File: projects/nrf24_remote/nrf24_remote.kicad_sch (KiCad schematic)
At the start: 74 parts

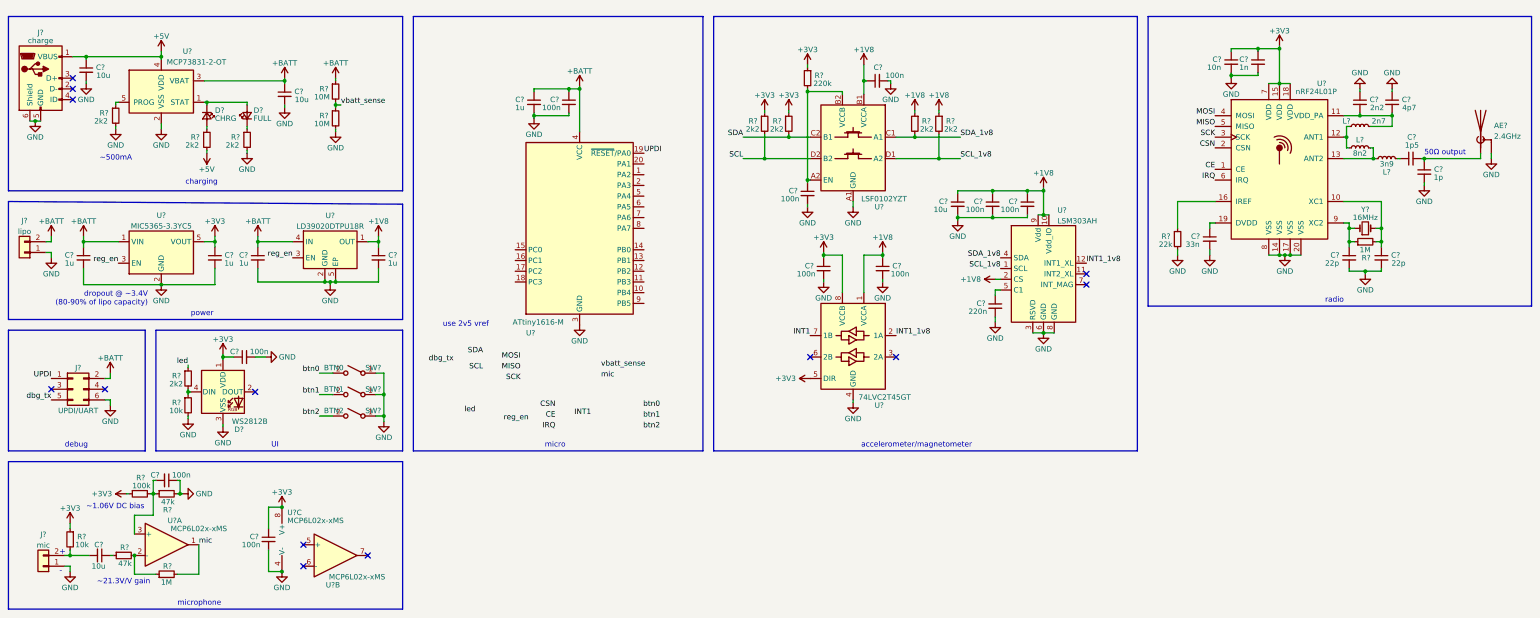
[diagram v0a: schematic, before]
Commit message: assigned nrf24_remote footprints
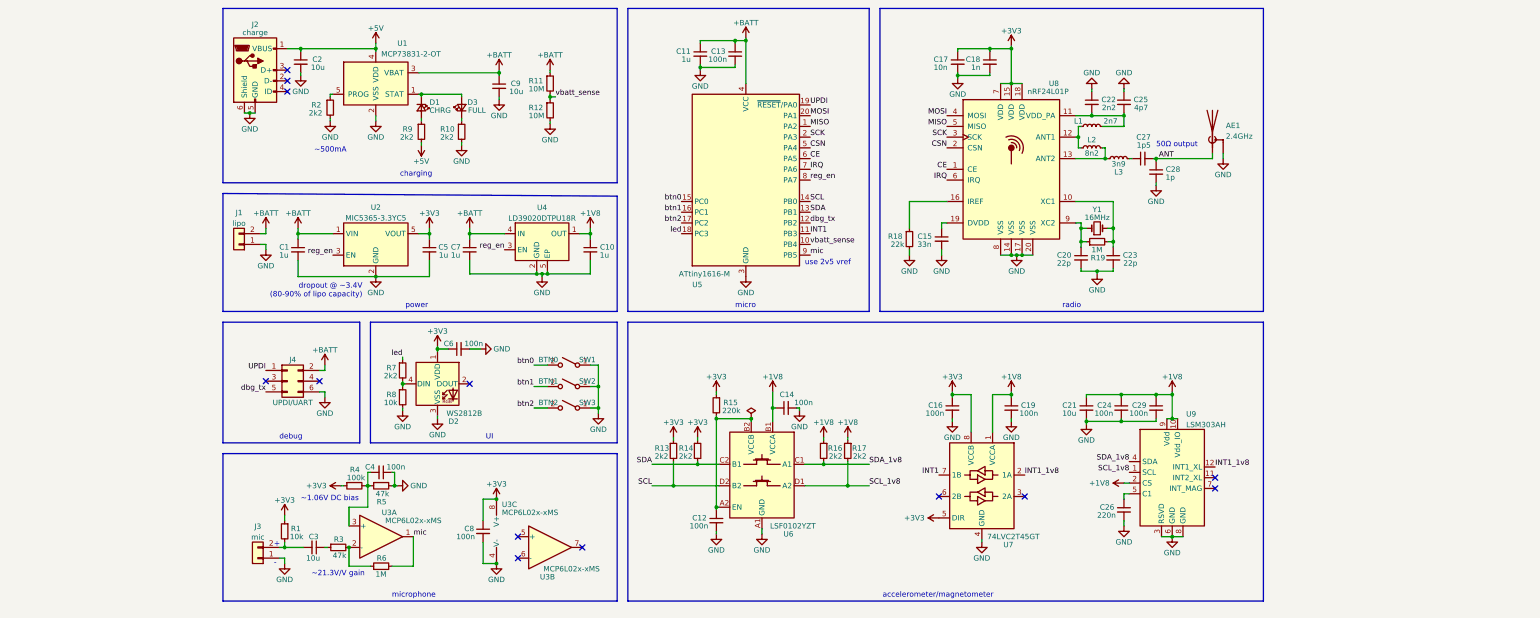
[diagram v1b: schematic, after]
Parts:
- AE1: renamed from AE?; footprint (none) -> RF_Antenna:Texas_SWRA117D_2.4GHz_Right
- C1, C10, C11, C12, C13, C14, C15, C16, C17, C18, C19, C2, C20, C21, C22, C23, C24, C25, C26, C27, C28, C29, C3, C4, C5, C6, C7, C8, C9: renamed from C?; footprint (none) -> Capacitor_SMD:C_0603_1608Metric
- D1, D3: renamed from D?; footprint (none) -> LED_SMD:LED_0603_1608Metric
- D2: renamed from D?; footprint (none) -> LED_SMD:LED_SK6812MINI_PLCC4_3.5x3.5mm_P1.75mm
- J1, J3: renamed from J?; footprint (none) -> Connector_PinHeader_2.00mm:PinHeader_1x02_P2.00mm_Vertical
- J2: renamed from J?; footprint (none) -> extraparts:USB_Micro-B_U254-05
- J4: renamed from J?; footprint (none) -> Connector:Tag-Connect_TC2030-IDC-NL_2x03_P1.27mm_Vertical
- L1, L2, L3: renamed from L?; footprint (none) -> Inductor_SMD:L_0603_1608Metric
- R1, R10, R11, R12, R13, R14, R15, R16, R17, R18, R19, R2, R3, R4, R5, R6, R7, R8, R9: renamed from R?; footprint (none) -> Resistor_SMD:R_0603_1608Metric
- SW1, SW2, SW3: renamed from SW?; footprint (none) -> extraparts:SW_SPST_EVPAF
- U7: renamed from U?; footprint (none) -> extraparts:NXP_XSON-8
- Y1: renamed from Y?; footprint (none) -> Crystal:Crystal_HC49-4H_Vertical
- gave numbers to parts that had none: 8
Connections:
- net CE: now also U5.6 (PA5)
- net CSN: now also U5.5 (PA4)
- net INT1: now also U5.11 (PB3)
- net IRQ: now also U5.7 (PA6)
- net MISO: now also U5.1 (PA2)
- net MOSI: now also U5.20 (PA1)
- net SCK: now also U5.2 (PA3)
- net SCL: now also U5.14 (PB0)
- net SDA: now also U5.13 (PB1)
- net btn0: now also U5.15 (PC0)
- net btn1: now also U5.16 (PC1)
- net btn2: now also U5.17 (PC2)
- net dbg_tx: now also U5.12 (PB2)
- net led: now also U5.18 (PC3)
- net mic: now also U5.9 (PB5)
- net reg_en: now also U5.8 (PA7)
- net vbatt_sense: now also U5.10 (PB4)
- net ANT: now reaches AE1.1 (A), C27.2, C28.1
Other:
- moved on the sheet: AE1, C1, C10, C11, C12, C13, C14, C15, C16, C17, C18, C19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

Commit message: finish nnrf24_remote layout
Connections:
- net +3V3: no longer C16.1, U7.5 (DIR), U7.8 (VCCB)
- net +BATT: now also C16.1, U7.5 (DIR), U7.8 (VCCB)
- net GND: now also U8.21 (EP)
- net INT1: now also U5.18 (PC3); no longer U5.11 (PB3)
- net btn0: now also U5.17 (PC2); no longer U5.15 (PC0)
- net btn2: now also U5.15 (PC0); no longer U5.17 (PC2)
- net led: now also U5.11 (PB3); no longer U5.18 (PC3)
- net mic: now also U5.8 (PA7); no longer U5.9 (PB5)
- net reg_en: now also U5.10 (PB4); no longer U5.8 (PA7)
- net vbatt_sense: now also U5.9 (PB5); no longer U5.10 (PB4)
- net XTAL-: now reaches C20.1, R19.1, U8.9 (XC2), Y1.1
- net XTAL+: now reaches C23.1, R19.2, U8.10 (XC1), Y1.2
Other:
- note added: "support shake-to-wake in sleep"
- moved on the sheet: C20, C23, R19, Y1

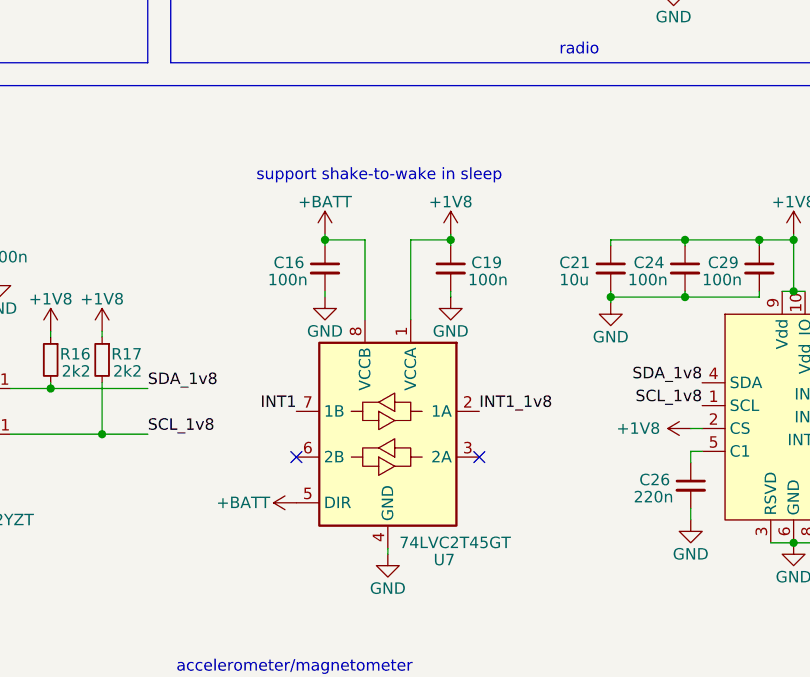
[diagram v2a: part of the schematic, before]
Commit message: update nrf24_remote
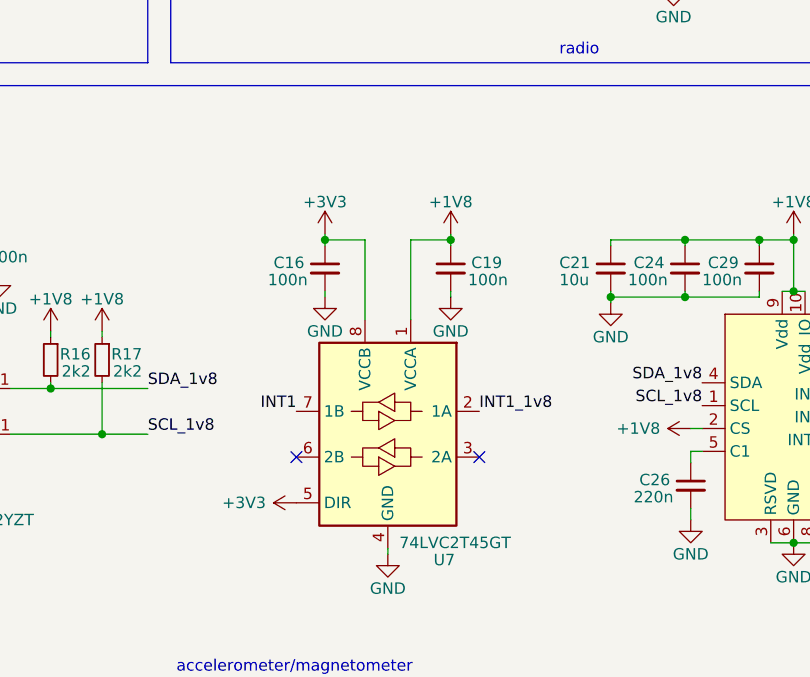
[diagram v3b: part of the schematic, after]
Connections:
- net +3V3: now also C16.1, U7.5 (DIR), U7.8 (VCCB)
- net +BATT: no longer C16.1, U7.5 (DIR), U7.8 (VCCB)
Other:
- note removed: "support shake-to-wake in sleep"
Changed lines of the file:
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@@
-    (effects (font (size 1.27 1.27)) (justify left bottom))
-  )
-  (text "support shake-to-wake in sleep" (at 248.285 158.115 0)
     (effects (font (size 1.27 1.27)) (justify left bottom))
   )
@@
     (pin "1")
     (pin "2")
-  )
-  (symbol (lib_id "power:+BATT") (at 255.905 163.83 0) (unit 1)
-    (in_bom yes) (on_board yes) (fields_autoplaced)
-    (property "Reference" "#PWR0101" (id 0) (at 255.905 167.64 0)
-      (effects (font (size 1.27 1.27)) hide)
-    )
-    (property "Value" "+BATT" (id 1) (at 255.905 160.2542 0))
-    (property "Footprint" "" (id 2) (at 255.905 163.83 0)
-      (effects (font (size 1.27 1.27)) hide)
-    )
-    (property "Datasheet" "" (id 3) (at 255.905 163.83 0)
-      (effects (font (size 1.27 1.27)) hide)
-    )
-    (pin "1")
   )
   (symbol (lib_id "Device:C_Small") (at 264.795 85.725 0) (unit 1)
@@
     (pin "1")
   )
+  (symbol (lib_id "power:+3V3") (at 255.905 163.83 0) (unit 1)
+    (in_bom yes) (on_board yes) (fields_autoplaced)
+    (property "Reference" "#PWR048" (id 0) (at 255.905 167.64 0)
+      (effects (font (size 1.27 1.27)) hide)
+    )
+    (property "Value" "+3V3" (id 1) (at 255.905 160.2542 0))
+    (property "Footprint" "" (id 2) (at 255.905 163.83 0)
+      (effects (font (size 1.27 1.27)) hide)
+    )
+    (property "Datasheet" "" (id 3) (at 255.905 163.83 0)
+      (effects (font (size 1.27 1.27)) hide)
+    )
+    (pin "1")
+  )
   (symbol (lib_id "power:+3V3") (at 200.025 163.83 0) (unit 1)
     (in_bom yes) (on_board yes) (fields_autoplaced)
@@
     (pin "1")
   )
+  (symbol (lib_id "power:+3V3") (at 252.73 193.675 90) (unit 1)
+    (in_bom yes) (on_board yes)
+    (property "Reference" "#PWR046" (id 0) (at 256.54 193.675 0)
+      (effects (font (size 1.27 1.27)) hide)
+    )
+    (property "Value" "+3V3" (id 1) (at 244.475 193.675 90)
+      (effects (font (size 1.27 1.27)) (justify right))
+    )
+    (property "Footprint" "" (id 2) (at 252.73 193.675 0)
+      (effects (font (size 1.27 1.27)) hide)
+    )
+    (property "Datasheet" "" (id 3) (at 252.73 193.675 0)
+      (effects (font (size 1.27 1.27)) hide)
+    )
+    (pin "1")
+  )
   (symbol (lib_id "power:+3V3") (at 195.58 174.625 0) (unit 1)
     (in_bom yes) (on_board yes) (fields_autoplaced)
@@
     (pin "2")
   )
-  (symbol (lib_id "power:+BATT") (at 252.73 193.675 90) (unit 1)
-    (in_bom yes) (on_board yes)
-    (property "Reference" "#PWR0102" (id 0) (at 256.54 193.675 0)
-      (effects (font (size 1.27 1.27)) hide)
-    )
-    (property "Value" "+BATT" (id 1) (at 243.84 193.675 90)
-      (effects (font (size 1.27 1.27)) (justify right))
-    )
-    (property "Footprint" "" (id 2) (at 252.73 193.675 0)
-      (effects (font (size 1.27 1.27)) hide)
-    )
-    (property "Datasheet" "" (id 3) (at 252.73 193.675 0)
-      (effects (font (size 1.27 1.27)) hide)
-    )
-    (pin "1")
-  )
   (symbol (lib_id "power:GND") (at 255.905 170.815 0) (unit 1)
     (in_bom yes) (on_board yes)
@@
       (reference "#PWR045") (unit 1) (value "GND") (footprint "")
     )
+    (path "/bfeb38e6-a6da-4c2b-ac60-547fd3945203"
+      (reference "#PWR046") (unit 1) (value "+3V3") (footprint "")
+    )
     (path "/0b26623c-5fff-4d73-95c0-50831e0c8eea"
       (reference "#PWR047") (unit 1) (value "GND") (footprint "")
     )
+    (path "/4744cdbc-fafd-47c0-a3ae-05ba361844ca"
+      (reference "#PWR048") (unit 1) (value "+3V3") (footprint "")
+    )
     (path "/fd0dc227-488e-4ad7-91f7-ef2a56ab3e1f"
       (reference "#PWR049") (unit 1) (value "GND") (footprint "")
@@
       (reference "#PWR065") (unit 1) (value "GND") (footprint "")
     )
-    (path "/07d092f8-21ed-49ae-97ff-11e5df0a0ab0"
-      (reference "#PWR0101") (unit 1) (value "+BATT") (footprint "")
-    )
-    (path "/fa4f6a28-9b9c-4d77-9e30-78c2d6b47031"
-      (reference "#PWR0102") (unit 1) (value "+BATT") (footprint "")
-    )
     (path "/98269ec4-1e87-4637-9006-7bf4d61ebbe7"

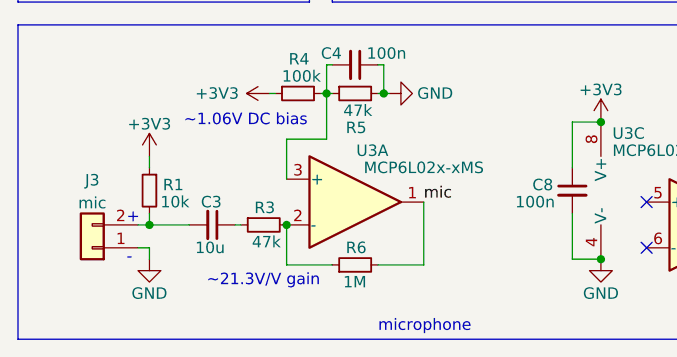
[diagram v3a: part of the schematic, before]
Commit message: update mic hpf
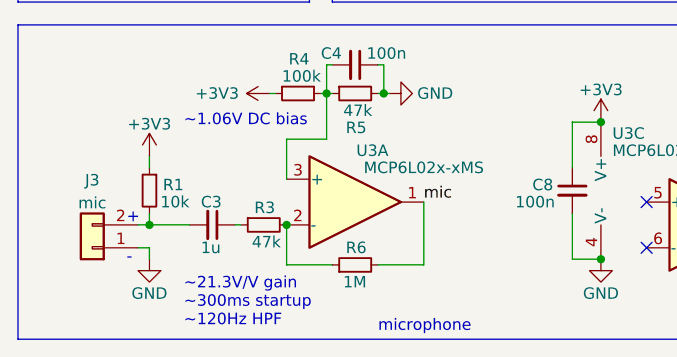
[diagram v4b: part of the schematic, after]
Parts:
- C3: value 10u -> 1u
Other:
- note added: "~21.3V/V gain ~300ms startup ~120Hz HPF"
- note removed: "~21.3V/V gain"
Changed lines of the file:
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@@
     (effects (font (size 1.27 1.27)) (justify left bottom))
   )
-  (text "~21.3V/V gain" (at 104.14 207.645 0)
+  (text "~21.3V/V gain\n~300ms startup\n~120Hz HPF" (at 101.6 212.09 0)
     (effects (font (size 1.27 1.27)) (justify left bottom))
   )
@@
       (effects (font (size 1.27 1.27)) (justify left))
     )
-    (property "Value" "10u" (id 1) (at 102.87 203.2 90)
+    (property "Value" "1u" (id 1) (at 103.505 203.2 90)
       (effects (font (size 1.27 1.27)) (justify left))
     )
@@
     )
     (path "/3cb73396-04cf-4c62-958e-28943074b6dc"
-      (reference "C3") (unit 1) (value "10u") (footprint "Capacitor_SMD:C_0603_1608Metric")
+      (reference "C3") (unit 1) (value "1u") (footprint "Capacitor_SMD:C_0603_1608Metric")
     )
     (path "/0570efea-f268-43b8-9595-c2d530b4e620"
